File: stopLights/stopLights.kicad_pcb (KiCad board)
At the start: 2 copper layers, 11 parts, among them J1 Conn_01x04

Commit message: Added traces.
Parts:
- J1: moved to B.Cu
- moved J1 39.0 mm to (149.9, 116.8), turned to 270 degrees
- moved R3 31.2 mm to (157.5, 106.7), turned to 270 degrees
- moved H3 29.0 mm to (165.1, 110.5)
- moved R1 27.3 mm to (152.4, 106.7), turned to 270 degrees
- moved R2 27.1 mm to (154.9, 106.7), turned to 270 degrees
- moved H4 23.2 mm to (165.1, 86.4)
- moved H2 22.0 mm to (142.2, 110.5)
- moved H1 12.4 mm to (142.2, 86.4)
- moved D1 8.98 mm to (154.9, 85.1), turned to 180 degrees
- moved D2 7.84 mm to (154.9, 92.7), turned to 180 degrees
- moved D3 7.17 mm to (154.9, 100.3), turned to 180 degrees
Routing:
- net Net-(D1-Pad1): track 0.00 -> 53.9 mm
- net Net-(D1-Pad2): track 0.00 -> 24.1 mm
- net Net-(D2-Pad2): track 0.00 -> 17.9 mm
- net Net-(D3-Pad2): track 0.00 -> 9.94 mm
- net Net-(J1-Pad4): track 0.00 -> 5.08 mm
- net Net-(J1-Pad3): track 0.00 -> 5.08 mm
- net Net-(J1-Pad2): track 0.00 -> 5.08 mm

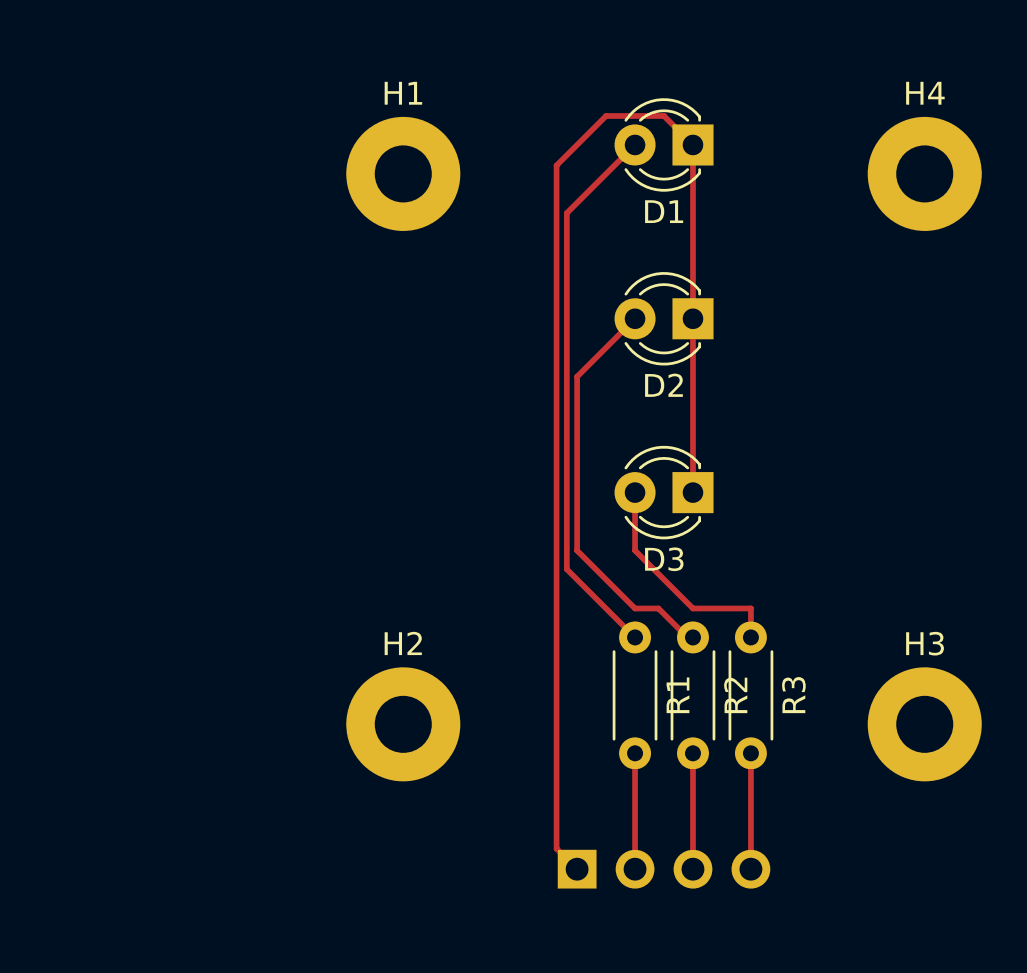
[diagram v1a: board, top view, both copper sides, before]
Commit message: reduced size of board.
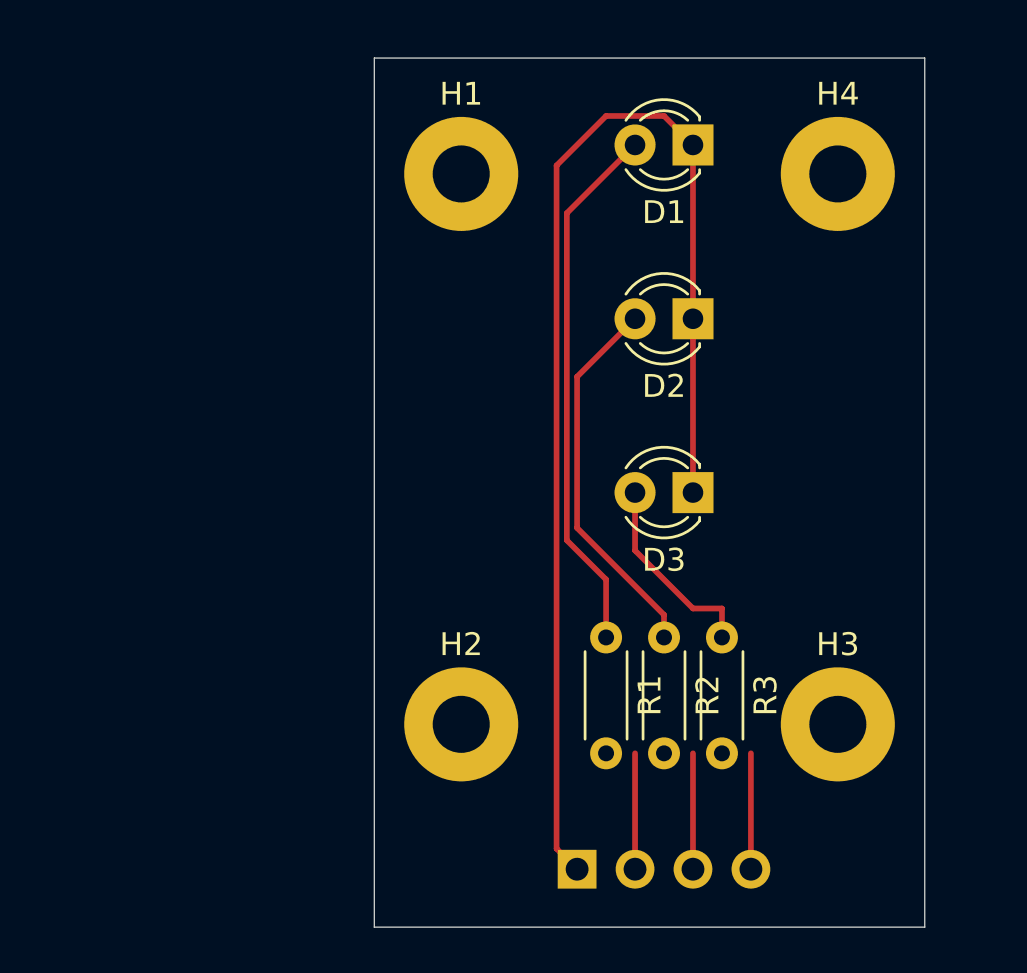
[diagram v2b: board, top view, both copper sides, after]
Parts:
- moved H3 3.81 mm to (161.3, 110.5)
- moved H4 3.81 mm to (161.3, 86.4)
- moved H1 2.54 mm to (144.8, 86.4)
- moved H2 2.54 mm to (144.8, 110.5)
- moved R1 1.27 mm to (151.1, 106.7)
- moved R2 1.27 mm to (153.7, 106.7)
- moved R3 1.27 mm to (156.2, 106.7)
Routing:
- net Net-(D3-Pad2): track 9.94 -> 8.67 mm
- net Net-(D2-Pad2): track 17.9 -> 16.8 mm
- net Net-(D1-Pad2): track 24.1 -> 23.5 mm
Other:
- board outline added: 24.1 x 38.1 mm
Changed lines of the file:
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@@
   (general
     (thickness 1.6)
-    (drawings 0)
+    (drawings 4)
     (tracks 23)
     (zones 0)
@@
   )
   (module Resistor_THT:R_Axial_DIN0204_L3.6mm_D1.6mm_P5.08mm_Horizontal (layer F.Cu)
-    (at 157.48 106.68 270)
+    (at 156.21 106.68 270)
     (descr "Resistor, Axial_DIN0204 series, Axial, Horizontal, pin pitch=5.08mm, 0.167W, length*diameter=3.6*1.6mm^2, http://cdn-reichelt.de/documents/datenblatt/B400/1_4W%23YAG.pdf")
     (tags "Resistor Axial_DIN0204 series Axial Horizontal pin pitch 5.08mm 0.167W length 3.6mm diameter 1.6mm")
@@
   )
   (module Resistor_THT:R_Axial_DIN0204_L3.6mm_D1.6mm_P5.08mm_Horizontal (layer F.Cu)
-    (at 154.94 106.68 270)
+    (at 153.67 106.68 270)
     (descr "Resistor, Axial_DIN0204 series, Axial, Horizontal, pin pitch=5.08mm, 0.167W, length*diameter=3.6*1.6mm^2, http://cdn-reichelt.de/documents/datenblatt/B400/1_4W%23YAG.pdf")
     (tags "Resistor Axial_DIN0204 series Axial Horizontal pin pitch 5.08mm 0.167W length 3.6mm diameter 1.6mm")
@@
   )
   (module Resistor_THT:R_Axial_DIN0204_L3.6mm_D1.6mm_P5.08mm_Horizontal (layer F.Cu)
-    (at 152.4 106.68 270)
+    (at 151.13 106.68 270)
     (descr "Resistor, Axial_DIN0204 series, Axial, Horizontal, pin pitch=5.08mm, 0.167W, length*diameter=3.6*1.6mm^2, http://cdn-reichelt.de/documents/datenblatt/B400/1_4W%23YAG.pdf")
     (tags "Resistor Axial_DIN0204 series Axial Horizontal pin pitch 5.08mm 0.167W length 3.6mm diameter 1.6mm")
@@
   )
   (module MountingHole:MountingHole_2.5mm_Pad (layer F.Cu)
-    (at 165.1 86.36)
+    (at 161.29 86.36)
     (descr "Mounting Hole 2.5mm")
     (tags "mounting hole 2.5mm")
@@
   )
   (module MountingHole:MountingHole_2.5mm_Pad (layer F.Cu)
-    (at 165.1 110.49)
+    (at 161.29 110.49)
     (descr "Mounting Hole 2.5mm")
     (tags "mounting hole 2.5mm")
@@
   )
   (module MountingHole:MountingHole_2.5mm_Pad (layer F.Cu)
-    (at 142.24 110.49)
+    (at 144.78 110.49)
     (descr "Mounting Hole 2.5mm")
     (tags "mounting hole 2.5mm")
@@
   )
   (module MountingHole:MountingHole_2.5mm_Pad (layer F.Cu)
-    (at 142.24 86.36)
+    (at 144.78 86.36)
     (descr "Mounting Hole 2.5mm")
     (tags "mounting hole 2.5mm")
@@
     )
   )
+  (gr_line (start 140.97 119.38) (end 140.97 81.28) (layer Edge.Cuts) (width 0.05))
+  (gr_line (start 165.1 119.38) (end 140.97 119.38) (layer Edge.Cuts) (width 0.05))
+  (gr_line (start 165.1 81.28) (end 165.1 119.38) (layer Edge.Cuts) (width 0.05))
+  (gr_line (start 140.97 81.28) (end 165.1 81.28) (layer Edge.Cuts) (width 0.05))
+  (segment (start 149.409989 102.419989) (end 151.13 104.14) (width 0.25) (layer F.Cu) (net 1))
   (segment (start 152.4 85.09) (end 149.409989 88.080011) (width 0.25) (layer F.Cu) (net 1))
-  (segment (start 149.409989 103.689989) (end 152.4 106.68) (width 0.25) (layer F.Cu) (net 1))
-  (segment (start 149.409989 88.080011) (end 149.409989 103.689989) (width 0.25) (layer F.Cu) (net 1))
+  (segment (start 149.409989 88.080011) (end 149.409989 102.419989) (width 0.25) (layer F.Cu) (net 1))
+  (segment (start 151.13 104.14) (end 151.13 106.68) (width 0.25) (layer F.Cu) (net 1))
   (segment (start 154.94 100.33) (end 154.94 92.71) (width 0.25) (layer F.Cu) (net 2))
   (segment (start 154.94 92.71) (end 154.94 85.09) (width 0.25) (layer F.Cu) (net 2))
@@
   (segment (start 153.67 83.82) (end 151.13 83.82) (width 0.25) (layer F.Cu) (net 2))
   (segment (start 154.94 85.09) (end 153.67 83.82) (width 0.25) (layer F.Cu) (net 2))
-  (segment (start 154.695001 106.68) (end 154.94 106.68) (width 0.25) (layer F.Cu) (net 3))
-  (segment (start 152.4 105.41) (end 153.425001 105.41) (width 0.25) (layer F.Cu) (net 3))
-  (segment (start 153.425001 105.41) (end 154.695001 106.68) (width 0.25) (layer F.Cu) (net 3))
+  (segment (start 153.425001 106.68) (end 153.67 106.68) (width 0.25) (layer F.Cu) (net 3))
+  (segment (start 149.86 101.880051) (end 153.67 105.690051) (width 0.25) (layer F.Cu) (net 3))
   (segment (start 152.4 92.71) (end 149.86 95.25) (width 0.25) (layer F.Cu) (net 3))
-  (segment (start 149.86 95.25) (end 149.86 102.87) (width 0.25) (layer F.Cu) (net 3))
-  (segment (start 149.86 102.87) (end 152.4 105.41) (width 0.25) (layer F.Cu) (net 3))
-  (segment (start 157.48 105.41) (end 157.48 106.68) (width 0.25) (layer F.Cu) (net 4))
+  (segment (start 149.86 95.25) (end 149.86 101.880051) (width 0.25) (layer F.Cu) (net 3))
+  (segment (start 153.67 105.690051) (end 153.67 106.68) (width 0.25) (layer F.Cu) (net 3))
+  (segment (start 156.21 105.41) (end 156.21 106.68) (width 0.25) (layer F.Cu) (net 4))
+  (segment (start 154.94 105.41) (end 156.21 105.41) (width 0.25) (layer F.Cu) (net 4))
   (segment (start 152.4 102.87) (end 154.94 105.41) (width 0.25) (layer F.Cu) (net 4))
-  (segment (start 154.94 105.41) (end 157.48 105.41) (width 0.25) (layer F.Cu) (net 4))
   (segment (start 152.4 100.33) (end 152.4 102.87) (width 0.25) (layer F.Cu) (net 4))
   (segment (start 157.48 111.76) (end 157.48 116.84) (width 0.25) (layer F.Cu) (net 5))

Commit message: Added text on Front silk layer.
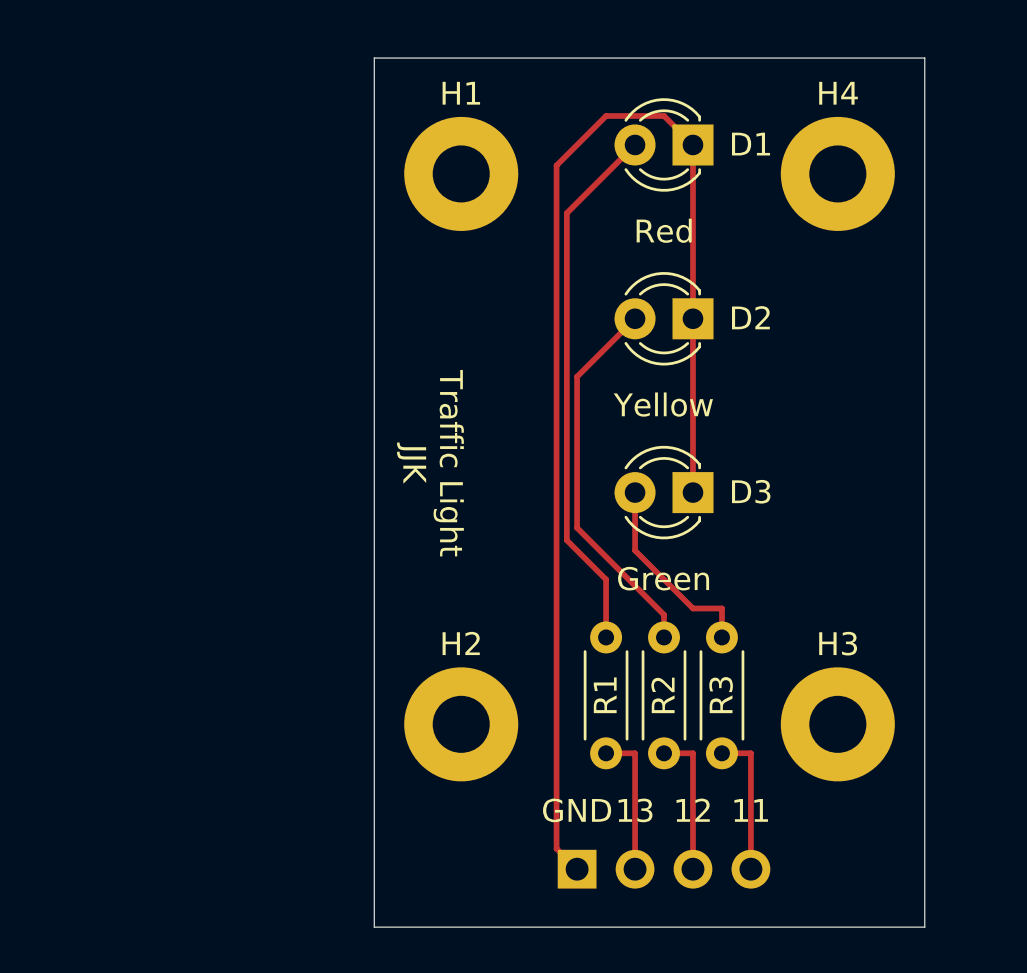
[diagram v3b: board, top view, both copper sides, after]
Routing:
- net Net-(J1-Pad3): track 5.08 -> 6.35 mm
- net Net-(J1-Pad2): track 5.08 -> 6.35 mm
- net Net-(J1-Pad4): track 5.08 -> 6.35 mm
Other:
- board text added: "11"
- board text added: "12"
- board text added: "13"
- board text added: "GND"
- board text added: "Green"
- board text added: "Red"
- board text added: "Traffic Light JJK"
- board text added: "Yellow"
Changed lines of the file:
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@@
   (general
     (thickness 1.6)
-    (drawings 4)
-    (tracks 23)
+    (drawings 12)
+    (tracks 26)
     (zones 0)
     (modules 11)
@@
     (descr "LED, diameter 3.0mm, 2 pins")
     (tags "LED diameter 3.0mm 2 pins")
-    (fp_text reference D2 (at 1.27 -2.96) (layer F.SilkS)
-      (effects (font (size 1 1) (thickness 0.15)))
-    )
-    (fp_text value LED (at 1.27 2.96) (layer F.Fab)
+    (fp_text reference D2 (at -2.54 0) (layer F.SilkS)
+      (effects (font (size 1 1) (thickness 0.15)))
+    )
+    (fp_text value LED (at 1.27 3.81) (layer F.Fab)
       (effects (font (size 1 1) (thickness 0.15)))
     )
@@
     (descr "LED, diameter 3.0mm, 2 pins")
     (tags "LED diameter 3.0mm 2 pins")
-    (fp_text reference D1 (at 1.27 -2.96) (layer F.SilkS)
-      (effects (font (size 1 1) (thickness 0.15)))
-    )
-    (fp_text value LED (at 1.27 2.96) (layer F.Fab)
+    (fp_text reference D1 (at -2.54 0) (layer F.SilkS)
+      (effects (font (size 1 1) (thickness 0.15)))
+    )
+    (fp_text value LED (at 1.27 2.54) (layer F.Fab)
       (effects (font (size 1 1) (thickness 0.15)))
     )
@@
     (descr "Resistor, Axial_DIN0204 series, Axial, Horizontal, pin pitch=5.08mm, 0.167W, length*diameter=3.6*1.6mm^2, http://cdn-reichelt.de/documents/datenblatt/B400/1_4W%23YAG.pdf")
     (tags "Resistor Axial_DIN0204 series Axial Horizontal pin pitch 5.08mm 0.167W length 3.6mm diameter 1.6mm")
-    (fp_text reference R3 (at 2.54 -1.92 90) (layer F.SilkS)
+    (fp_text reference R3 (at 2.54 0 90) (layer F.SilkS)
       (effects (font (size 1 1) (thickness 0.15)))
     )
@@
     (descr "Resistor, Axial_DIN0204 series, Axial, Horizontal, pin pitch=5.08mm, 0.167W, length*diameter=3.6*1.6mm^2, http://cdn-reichelt.de/documents/datenblatt/B400/1_4W%23YAG.pdf")
     (tags "Resistor Axial_DIN0204 series Axial Horizontal pin pitch 5.08mm 0.167W length 3.6mm diameter 1.6mm")
-    (fp_text reference R2 (at 2.54 -1.92 90) (layer F.SilkS)
+    (fp_text reference R2 (at 2.54 0 90) (layer F.SilkS)
       (effects (font (size 1 1) (thickness 0.15)))
     )
@@
     (descr "Resistor, Axial_DIN0204 series, Axial, Horizontal, pin pitch=5.08mm, 0.167W, length*diameter=3.6*1.6mm^2, http://cdn-reichelt.de/documents/datenblatt/B400/1_4W%23YAG.pdf")
     (tags "Resistor Axial_DIN0204 series Axial Horizontal pin pitch 5.08mm 0.167W length 3.6mm diameter 1.6mm")
-    (fp_text reference R1 (at 2.54 -1.92 90) (layer F.SilkS)
+    (fp_text reference R1 (at 2.54 0 90) (layer F.SilkS)
       (effects (font (size 1 1) (thickness 0.15)))
     )
@@
     (descr "LED, diameter 3.0mm, 2 pins")
     (tags "LED diameter 3.0mm 2 pins")
-    (fp_text reference D3 (at 1.27 -2.96) (layer F.SilkS)
-      (effects (font (size 1 1) (thickness 0.15)))
-    )
-    (fp_text value LED (at 1.27 2.96) (layer F.Fab)
+    (fp_text reference D3 (at -2.54 0) (layer F.SilkS)
+      (effects (font (size 1 1) (thickness 0.15)))
+    )
+    (fp_text value LED (at 1.27 5.08) (layer F.Fab)
       (effects (font (size 1 1) (thickness 0.15)))
     )
@@
       (rotate (xyz 0 0 0))
     )
+  )
+  (gr_text 11 (at 157.48 114.3) (layer F.SilkS)
+    (effects (font (size 1 1) (thickness 0.15)))
+  )
+  (gr_text 12 (at 154.94 114.3) (layer F.SilkS)
+    (effects (font (size 1 1) (thickness 0.15)))
+  )
+  (gr_text "13\n" (at 152.4 114.3) (layer F.SilkS)
+    (effects (font (size 1 1) (thickness 0.15)))
+  )
+  (gr_text "Traffic Light \nJJK" (at 143.51 99.06 -90) (layer F.SilkS)
+    (effects (font (size 1 1) (thickness 0.15)))
+  )
+  (gr_text GND (at 149.86 114.3) (layer F.SilkS)
+    (effects (font (size 1 1) (thickness 0.15)))
+  )
+  (gr_text Red (at 153.67 88.9) (layer F.SilkS)
+    (effects (font (size 1 1) (thickness 0.15)))
+  )
+  (gr_text "Yellow\n" (at 153.67 96.52) (layer F.SilkS)
+    (effects (font (size 1 1) (thickness 0.15)))
+  )
+  (gr_text Green (at 153.67 104.14) (layer F.SilkS)
+    (effects (font (size 1 1) (thickness 0.15)))
   )
   (gr_line (start 140.97 119.38) (end 140.97 81.28) (layer Edge.Cuts) (width 0.05))
@@
   (segment (start 152.4 100.33) (end 152.4 102.87) (width 0.25) (layer F.Cu) (net 4))
   (segment (start 157.48 111.76) (end 157.48 116.84) (width 0.25) (layer F.Cu) (net 5))
+  (segment (start 157.48 111.76) (end 156.21 111.76) (width 0.25) (layer F.Cu) (net 5))
   (segment (start 154.94 111.76) (end 154.94 116.84) (width 0.25) (layer F.Cu) (net 6))
+  (segment (start 154.94 111.76) (end 153.67 111.76) (width 0.25) (layer F.Cu) (net 6))
   (segment (start 152.4 111.76) (end 152.4 116.84) (width 0.25) (layer F.Cu) (net 7))
+  (segment (start 152.4 111.76) (end 151.13 111.76) (width 0.25) (layer F.Cu) (net 7))
 )
